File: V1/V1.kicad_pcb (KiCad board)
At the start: 4 copper layers, 46.7 x 47.2 mm, 102 parts, among them J1 AudioJack3_Ground, J2 AudioJack3_Ground, J3 AudioJack3_Ground, J4 USB_C_Receptacle_PowerOnly_6P, J5 Conn_01x08_Socket, J6 Conn_01x02_Socket, J7 AudioJack3_Ground, U1 ADS1299, U2 REF5025AIDR, U6 LT3045xMSE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

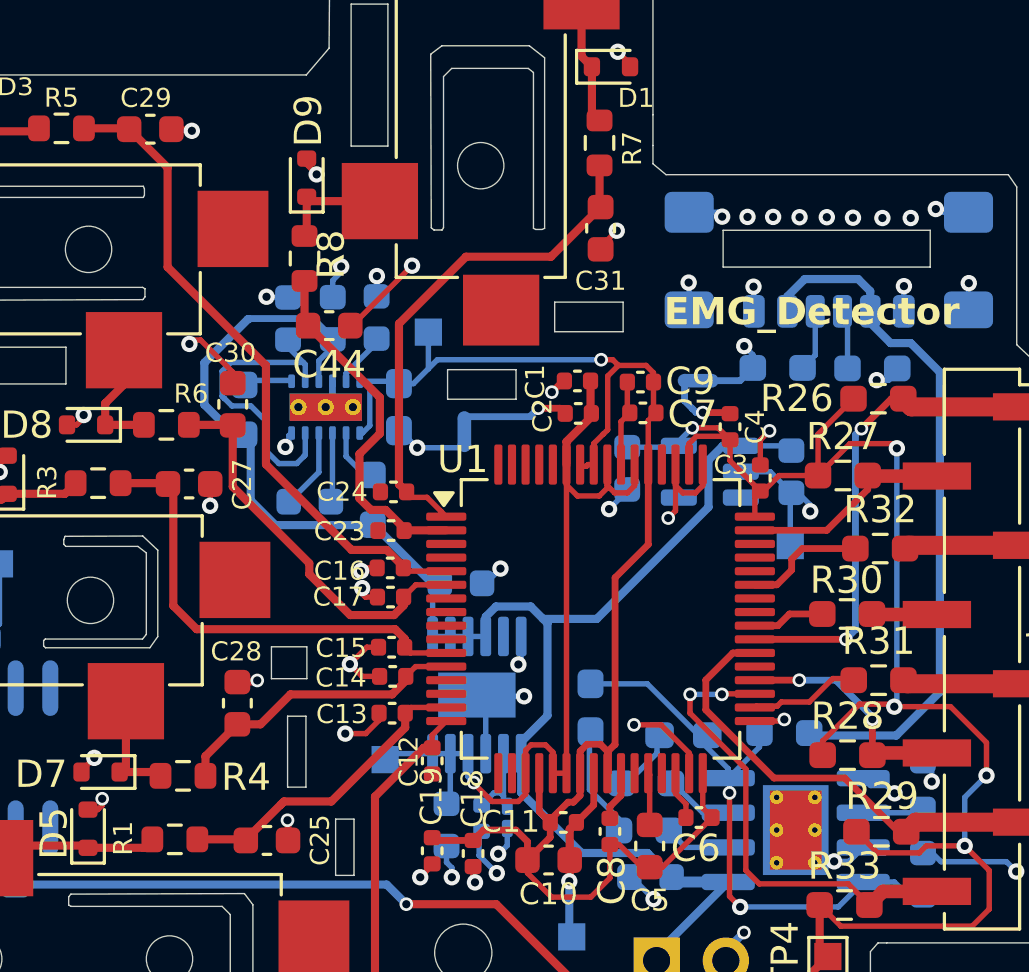
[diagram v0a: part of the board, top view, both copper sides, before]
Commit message: all tracks routing done
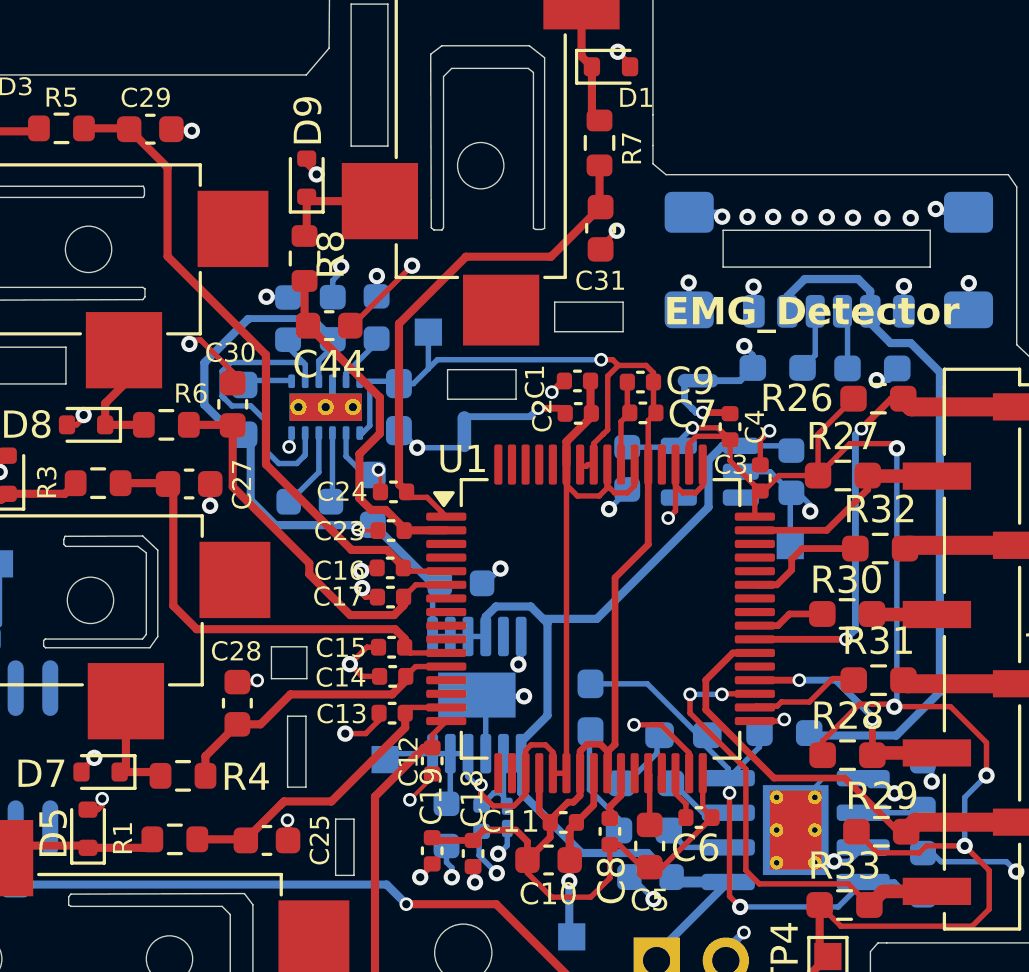
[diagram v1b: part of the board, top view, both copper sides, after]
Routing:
- net GND: track 64.7 -> 86.3 mm, vias 53 -> 56

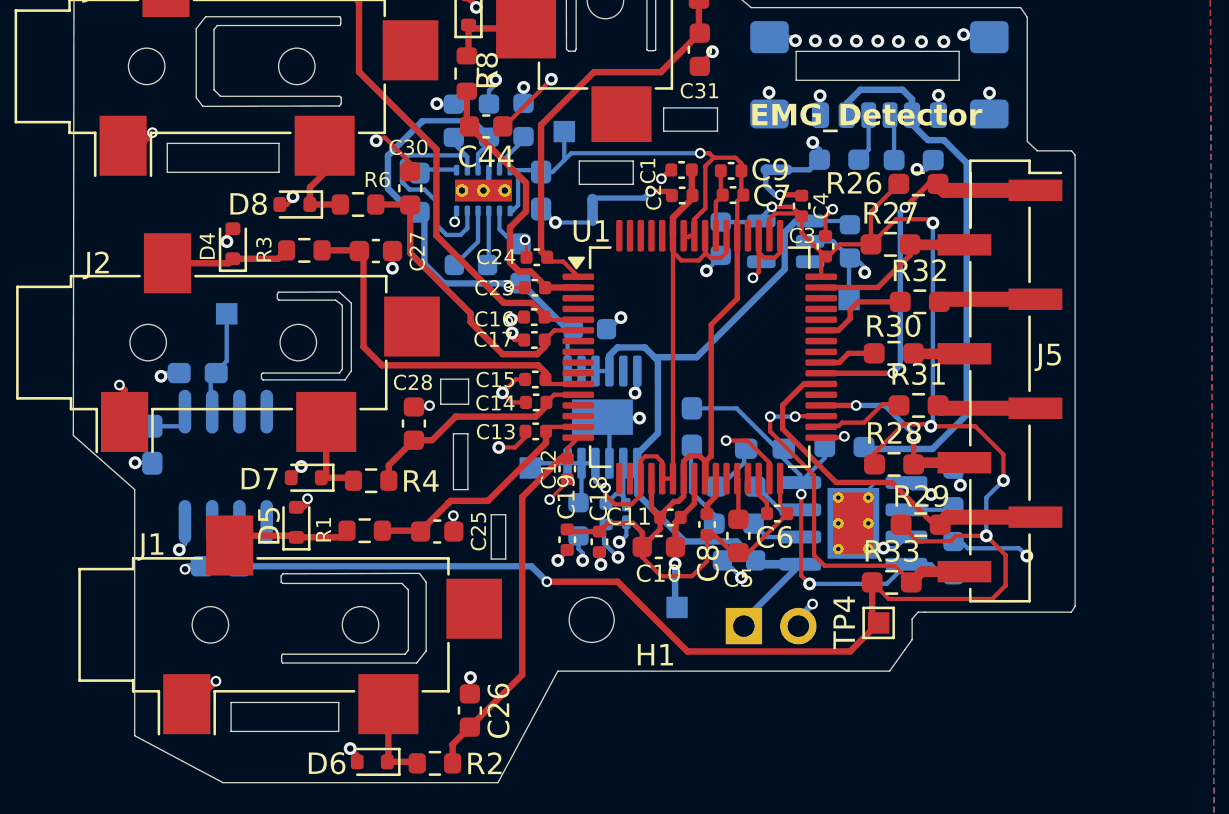
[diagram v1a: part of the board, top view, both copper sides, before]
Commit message: pcb design updated based on the suggestions.
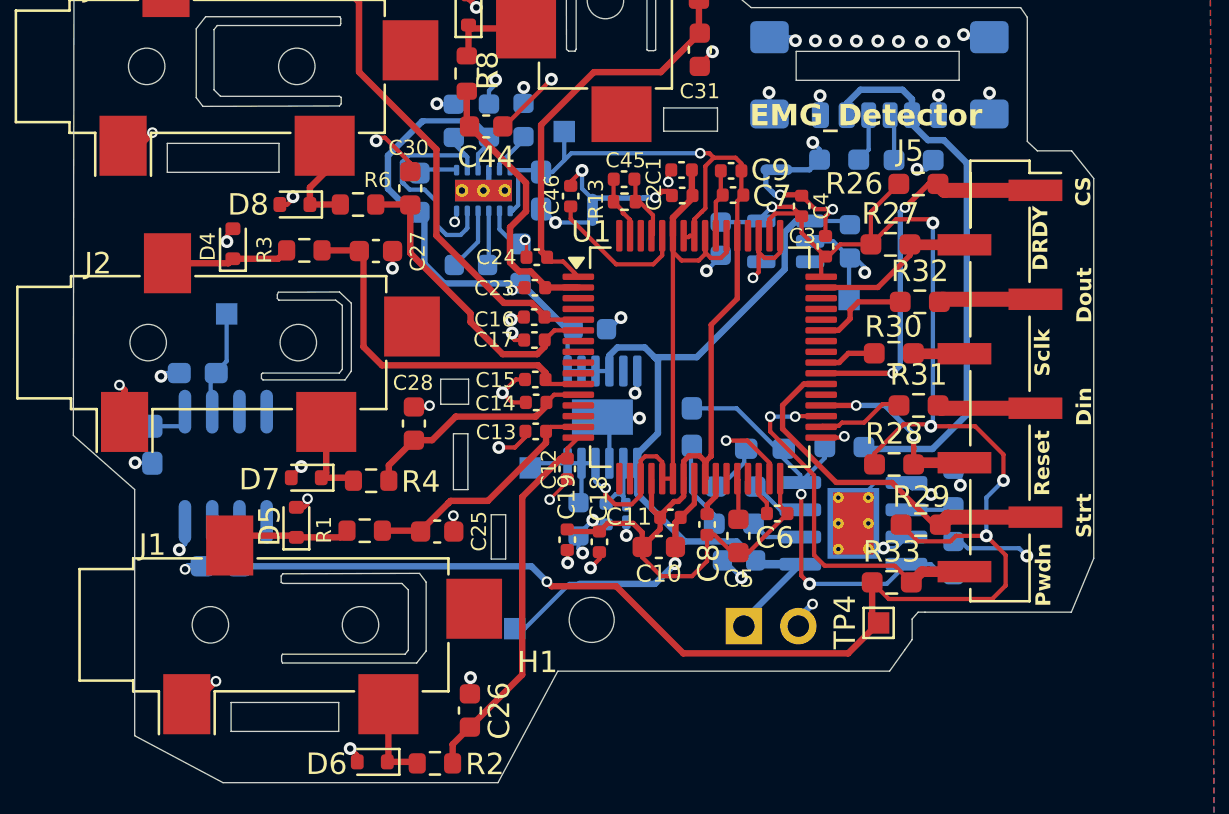
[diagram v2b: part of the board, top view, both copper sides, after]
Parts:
- added C45: 1.5nF, Capacitor_SMD:C_0402_1005Metric, F.Cu at (147.2, 85.8)
- added C46: 1nF, Capacitor_SMD:C_0402_1005Metric, F.Cu at (144.7, 86.6)
- added R13: 1M, Resistor_SMD:R_0402_1005Metric, F.Cu at (147.2, 86.9)
- C12, C13, C14, C15, C16, C17, C23, C24: value 1nF -> 10nF
- moved TP1 7.63 mm to (142.1, 106.8)
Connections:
- U1 pad 60: unconnected-(U1-BIASREF-Pad60) -> Net-(U1-BIASREF)
- U1 pad 61: unconnected-(U1-BIASINV-Pad61) -> Net-(U1-BIASINV)
- U1 pad 63: unconnected-(U1-BIASOUT-Pad63) -> Net-(U1-BIASOUT)
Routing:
- net GNDD: track 9.94 -> 25.9 mm
- net GNDA: track 23.1 -> 33.0 mm
- net Net-(U1-BIASREF): track 0.00 -> 6.81 mm
- net Net-(U1-VREFP): track 6.42 -> 13.1 mm
- net Net-(U1-BIASINV): track 0.00 -> 3.14 mm
- net Net-(U1-BIASOUT): track 0.00 -> 2.98 mm
- net GND: track 86.3 -> 88.8 mm, vias 56 -> 57
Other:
- board size 46.7 x 47.2 mm -> 47.6 x 47.2 mm
- board text added: "BATT"
- board text added: "CS"
- board text added: "DRDY"
- board text added: "Din"
- board text added: "Dout"
- board text added: "Pwdn"
- board text added: "Reset"
- board text added: "Sclk"
- board text added: "Strt"
